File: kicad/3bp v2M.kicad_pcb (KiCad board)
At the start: 2 copper layers, 29 x 38.5 mm, 100 parts, among them CON1 MD-90SM, U1 TL972IDR, U2 THS7374IPWR

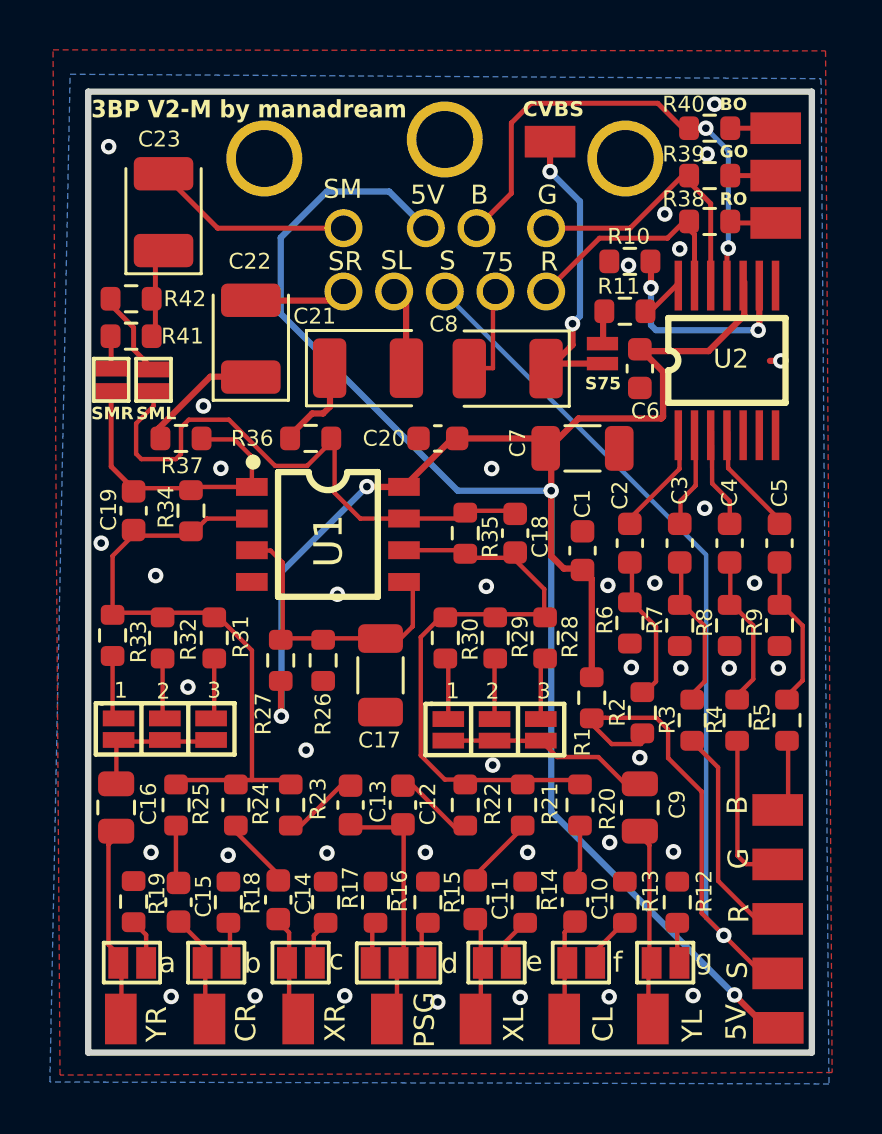
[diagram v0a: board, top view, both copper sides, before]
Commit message: Added 4 channel op amp to restore mono and cleaned up repo
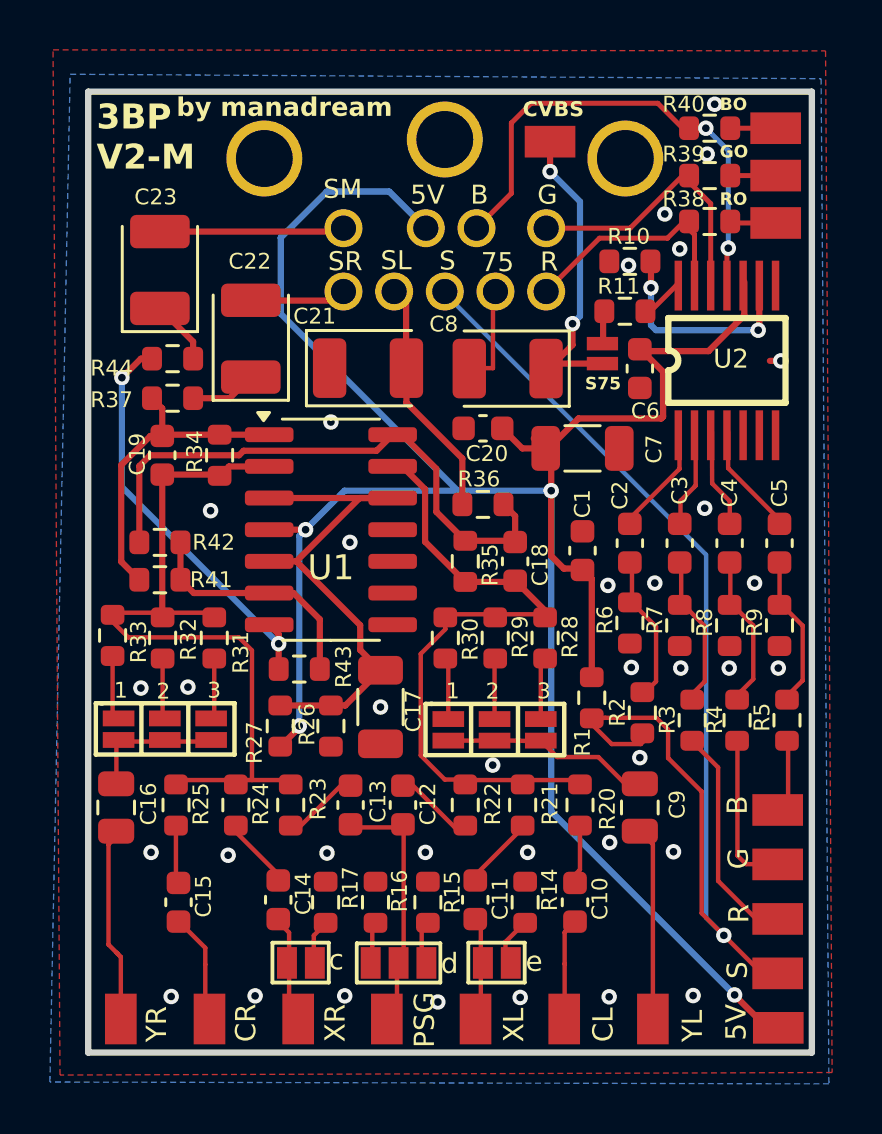
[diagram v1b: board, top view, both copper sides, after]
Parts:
- removed the ? at (127.0, 93.5)
- removed the ? at (125.3, 93.5)
- removed the ? at (127.0, 92.6)
- removed the ? at (125.3, 92.6)
- removed R12, R19: 2.20k, Resistor_SMD:R_0603_1608Metric
- removed R13, R18: 75.0, Resistor_SMD:R_0603_1608Metric
- removed a, b, f, g: JUMPER_PADSX2, easyeda:JUMPER_PADSX2
- added R43: 4.7k, Resistor_SMD:R_0603_1608Metric, F.Cu at (132.8, 104.6)
- added R44: 330, Resistor_SMD:R_0603_1608Metric, F.Cu at (127.8, 92.2)
- R41, R42: value 1k -> 10k
- U1: value TL972IDR -> TL974IDR; footprint easyeda:DMP-8 -> Package_SO:SOIC-14_3.9x8.7mm_P1.27mm
- moved R41 9.84 mm to (127.3, 101.1)
- moved R42 9.84 mm to (127.3, 99.6)
- moved R36 7.40 mm to (140.2, 98.0)
- moved R26 2.65 mm to (134.1, 106.9)
- moved R27 2.63 mm to (132.1, 106.9)
- moved C19 2.50 mm to (127.3, 96.1)
- moved R34 2.50 mm to (129.6, 96.1)
- moved C23 2.32 mm to (127.3, 88.6)
- moved C20 1.85 mm to (140.2, 95.0)
- moved R37 1.65 mm to (127.8, 93.8), turned to 0 degrees
- moved C17 1.27 mm to (136.1, 106.2)
- moved C18 1.13 mm to (141.5, 100.3)
- moved R35 1.13 mm to (139.5, 100.3)
- moved U1 0.22 mm to (134.1, 99.1), turned to 0 degrees
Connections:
- C17 pad 1: S$33979 -> OPAVREF
- C18 pad 1: LEFT -> LOUT
- C19 pad 2: RIGHT -> ROUT
- R26 pad 2: S$33979 -> OPAVREF
- R27 pad 2: S$33979 -> OPAVREF
- R34 pad 2: RIGHT -> ROUT
- R35 pad 1: LEFT -> LOUT
- R36 pad 2: LEFT -> LOUT
- R37 pad 1: RIGHT -> ROUT
- R41 pad 1: SM -> MONO
- R41 pad 2: RIGHT -> ROUT
- R42 pad 1: SM -> MONO
- R42 pad 2: LEFT -> LOUT
- U1 pad 1: RIGHT -> ROUT
- U1 pad 3: S$33979 -> OPAVREF
- U1 pad 4: GND -> +5V
- U1 pad 5: S$33979 -> OPAVREF
- U1 pad 6: LEFT -> MONO
- U1 pad 7: LEFT -> MOUT
- U1 pad 8: +5V -> (no net)
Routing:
- net LEFT: track 51.1 -> 26.9 mm
- net LOUT: track 0.00 -> 23.1 mm
- net OPAVREF: track 0.00 -> 22.3 mm
- net MOUT: track 0.00 -> 16.7 mm, vias 0 -> 2
- net ROUT: track 0.00 -> 13.1 mm
- net S$33979: track 12.4 -> 0.00 mm
- net MONO: track 0.00 -> 9.74 mm
- net RIGHT: track 38.2 -> 31.0 mm
- net SL: track 7.17 -> 9.72 mm
- net SR: track 9.27 -> 6.94 mm
- net SCD-LEFT: track 8.33 -> 6.04 mm
- net SCD-RIGHT: track 8.25 -> 6.51 mm
- net SM: track 11.7 -> 9.99 mm
- net YM-RIGHT: track 21.2 -> 19.5 mm
- net YM-LEFT: track 24.8 -> 23.3 mm
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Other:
- board text added: "3BP V2-M"
- board text added: "M1va0-6.5 = 1 M1va7 = 2 M2va0-1.8 = 2, c, e M2va2-2.3 = 1, d-left M2va3 = 2 M2va4 = 3, d-right M3va1-2 = 3, c, d-right, e"
- board text added: "by manadream"
- board text removed: "3BP V2-M by manadream"
- board text removed: "M1va0-6.5 = 1 M1va7 = 2 M2va0-1.8 = 2, c, e M2va2-2.3= 1, d-left M2va3 = 2 M2va4 = 3, d-right M3va1/2= 3, b, c, d-right, e, f"
- board text removed: "SML"
- board text removed: "SMR"
